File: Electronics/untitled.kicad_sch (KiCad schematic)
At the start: 23 parts

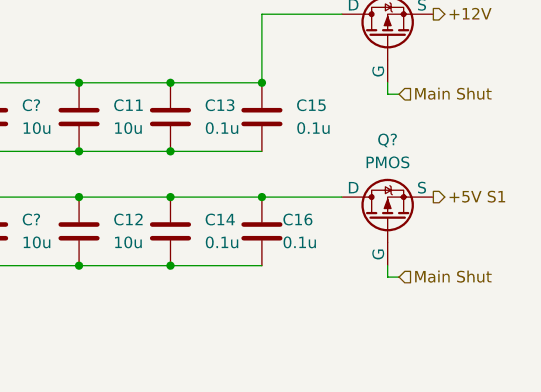
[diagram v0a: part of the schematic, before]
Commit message: Starting the Sheet connections
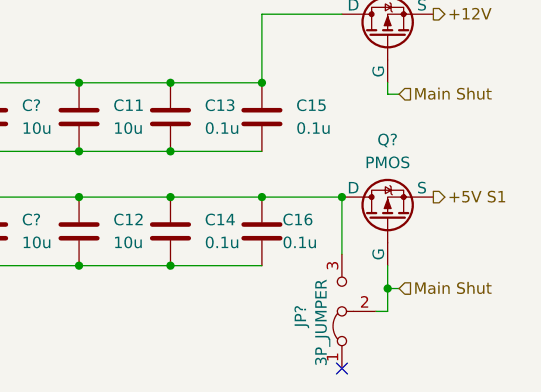
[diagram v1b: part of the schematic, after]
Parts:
- added JP?: 3P_JUMPER, symbol Jumper:Jumper_3_Bridged12
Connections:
- net Main Shut: now also JP?.2 (C)
- net at C12.1, C14.1, C16.1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: now also JP?.3 (B)
- no-connect marks 0 -> 1
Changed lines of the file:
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@@
 	(paper "A5")
 	(junction
+		(at 176.53 63.5)
+		(diameter 0)
+		(color 0 0 0 0)
+	)
+	(junction
 		(at 152.4 48.26)
 		(diameter 0)
@@
 	)
 	(junction
+		(at 171.45 53.34)
+		(diameter 0)
+		(color 0 0 0 0)
+	)
+	(junction
 		(at 121.92 40.64)
 		(diameter 0)
@@
 		(color 0 0 0 0)
 	)
+	(no_connect
+		(at 171.45 72.39)
+	)
 	(wire
 		(pts
@@
 	(wire
 		(pts
+			(xy 176.53 63.5) (xy 176.53 66.04)
+		)
+		(stroke
+			(width 0)
+			(type default)
+		)
+	)
+	(wire
+		(pts
 			(xy 121.92 40.64) (xy 111.76 40.64)
 		)
@@
 	(wire
 		(pts
+			(xy 171.45 59.69) (xy 171.45 53.34)
+		)
+		(stroke
+			(width 0)
+			(type default)
+		)
+	)
+	(wire
+		(pts
 			(xy 62.23 55.88) (xy 62.23 45.72)
 		)
@@
 	(wire
 		(pts
-			(xy 176.53 62.23) (xy 177.8 62.23)
+			(xy 176.53 63.5) (xy 177.8 63.5)
 		)
 		(stroke
@@
 	(wire
 		(pts
-			(xy 176.53 60.96) (xy 176.53 62.23)
+			(xy 176.53 60.96) (xy 176.53 63.5)
 		)
 		(stroke
@@
 		(pts
 			(xy 78.74 60.96) (xy 90.17 60.96)
+		)
+		(stroke
+			(width 0)
+			(type default)
+		)
+	)
+	(wire
+		(pts
+			(xy 176.53 66.04) (xy 175.26 66.04)
 		)
 		(stroke
@@
 	(hierarchical_label "Main Shut"
 		(shape input)
-		(at 177.8 62.23 0)
+		(at 177.8 63.5 0)
 		(effects
 			(font
@@
 		(on_board yes)
 		(dnp no)
-		(fields_autoplaced yes)
 		(property "Reference" "J?"
 			(at 52.07 33.02 0)
@@
 					(unit 1)
 				)
+			)
+		)
+	)
+	(symbol
+		(lib_id "Jumper:Jumper_3_Bridged12")
+		(at 171.45 66.04 90)
+		(unit 1)
+		(exclude_from_sim no)
+		(in_bom no)
+		(on_board yes)
+		(dnp no)
+		(property "Reference" "JP?"
+			(at 166.878 67.818 0)
+			(effects
+				(font
+					(size 1.27 1.27)
+				)
+				(justify left)
+			)
+		)
+		(property "Value" "3P_JUMPER"
+			(at 169.164 72.136 0)
+			(effects
+				(font
+					(size 1.27 1.27)
+				)
+				(justify left)
+			)
+		)
+		(property "Footprint" ""
+			(at 171.45 66.04 0)
+			(effects
+				(font
+					(size 1.27 1.27)
+				)
+				(hide yes)
+			)
+		)
+		(property "Datasheet" "~"
+			(at 171.45 66.04 0)
+			(effects
+				(font
+					(size 1.27 1.27)
+				)
+				(hide yes)
+			)
+		)
+		(property "Description" "Jumper, 3-pole, pins 1+2 closed/bridged"
+			(at 171.45 66.04 0)
+			(effects
+				(font
+					(size 1.27 1.27)
+				)
+				(hide yes)
+			)
+		)
+		(pin "3"
+		)
+		(pin "1"
+		)
+		(pin "2"
+		)
+		(instances
+			(project "CM5 Nas"
+				(path "/0650c7a8-acba-429c-9f8e-eec0baf0bc1c/fede4c36-00cc-4d3d-b71c-5243ba232202/ff10faca-55ce-4526-b63b-58be6b3f0345"
+					(reference "JP?")
+					(unit 1)
+				)

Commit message: Footprints Selected
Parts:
- removed JP?: 3P_JUMPER, symbol Jumper:Jumper_3_Bridged12
- added D5, D6: LED Green, LED_SMD:LED_0603_1608Metric, symbol Device:LED
- added R11, R12: 1K, Resistor_SMD:R_0603_1608Metric, symbol Device:R_Small
- added TP5: TestPoint, TestPoint:TestPoint_Pad_1.0x1.0mm, symbol Connector:TestPoint
- C10, C12, C13, C8: renamed from C?; footprint (none) -> Capacitor_SMD:C_0603_1608Metric
- C11: renamed from C8; footprint (none) -> Capacitor_SMD:C_0603_1608Metric
- C14: renamed from C11; footprint (none) -> Capacitor_SMD:C_0603_1608Metric
- C15: renamed from C12; footprint (none) -> Capacitor_SMD:C_0603_1608Metric
- C16: renamed from C13; footprint (none) -> Capacitor_SMD:C_0603_1608Metric
- C17: renamed from C14; footprint (none) -> Capacitor_SMD:C_0603_1608Metric
- C18: renamed from C15; footprint (none) -> Capacitor_SMD:C_0603_1608Metric
- C19: renamed from C16; footprint (none) -> Capacitor_SMD:C_0603_1608Metric
- C4: renamed from C1; value 1000n -> 1u; footprint (none) -> Capacitor_SMD:C_0603_1608Metric
- C5: renamed from C2; value 1000n -> 1u; footprint (none) -> Capacitor_SMD:C_0603_1608Metric
- C6: renamed from C3; footprint (none) -> Capacitor_SMD:C_0603_1608Metric
- C7: renamed from C4; footprint (none) -> Capacitor_SMD:C_0603_1608Metric
- C9: renamed from C6; footprint (none) -> Capacitor_SMD:C_0603_1608Metric
- D3: renamed from D1; footprint (none) -> SMBJ12A:SMBJ12A
- D4: renamed from D2; footprint (none) -> SMBJ5.0A:SMBJ5.0A
- F1, F2: footprint (none) -> RGEF1200:RGEF1200
- J15: renamed from J?; footprint 4DBP10803 -> 4DB-P108-03:4DBP10803
- Q2, Q3: renamed from Q?; footprint (none) -> IRF7425TRPBF:SOIC127P600X175-8N
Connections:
- net +12V: now also C10.1, C12.1, C14.1, C16.1, C18.1, C4.1, C6.1, C8.1, D3.2 (A2), F1.2, R11.2, TP5.1; no longer Q2.3 (S)
- net +5V S1: now also C11.1, C13.1, C15.1, C17.1, C19.1, C5.1, C7.1, C9.1, D4.2 (A2), F2.2; no longer Q3.3 (S)
- net at C11.2, C13.2, C15.2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: now also R12.2
- net at J15.2: now also Q3.1 (D); no longer F2.1
- net at J15.3: now also Q2.1 (D); no longer F1.1
- new net: D5.2 (A), R11.1
- new net: D6.2 (A), R12.1
- new net: F2.1, Q3.3 (S)
- new net: F1.1, Q2.3 (S)
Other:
- moved on the sheet: J15, Q2, Q3

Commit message: Footprints selected, Hiracicle connections created, Pcb next
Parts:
- removed C6, C7: 1000u, Capacitor_SMD:C_0603_1608Metric, symbol Device:C
- removed Q2, Q3: PMOS, IRF7425TRPBF:SOIC127P600X175-8N, symbol Simulation_SPICE:PMOS
- added C13, C5: 1000u, EEE0JA152UAP:EEE0JA152UAP, symbol Device:C_Polarized
- added TP4, TP5: TestPoint, TestPoint:TestPoint_Pad_1.0x1.0mm, symbol Connector:TestPoint
- C10: renamed from C16; value 0.1u -> 100n; footprint Capacitor_SMD:C_0603_1608Metric -> Capacitor_SMD:C_0402_1005Metric
- C11: renamed from C18; value 0.1u -> 100n; footprint Capacitor_SMD:C_0603_1608Metric -> Capacitor_SMD:C_0402_1005Metric
- C12: renamed from C5; footprint Capacitor_SMD:C_0603_1608Metric -> Capacitor_SMD:C_1210_3225Metric
- C14: renamed from C9; footprint Capacitor_SMD:C_0603_1608Metric -> Capacitor_SMD:C_1210_3225Metric
- C15: renamed from C11; footprint Capacitor_SMD:C_0603_1608Metric -> Capacitor_SMD:C_1210_3225Metric
- C16: renamed from C13; footprint Capacitor_SMD:C_0603_1608Metric -> Capacitor_SMD:C_1210_3225Metric
- C17: renamed from C15; footprint Capacitor_SMD:C_0603_1608Metric -> Capacitor_SMD:C_1210_3225Metric
- C18: renamed from C17; value 0.1u -> 100n; footprint Capacitor_SMD:C_0603_1608Metric -> Capacitor_SMD:C_0402_1005Metric
- C19: value 0.1u -> 100n; footprint Capacitor_SMD:C_0603_1608Metric -> Capacitor_SMD:C_0402_1005Metric
- C4: footprint Capacitor_SMD:C_0603_1608Metric -> Capacitor_SMD:C_1210_3225Metric
- C6: renamed from C8; footprint Capacitor_SMD:C_0603_1608Metric -> Capacitor_SMD:C_1210_3225Metric
- C7: renamed from C10; footprint Capacitor_SMD:C_0603_1608Metric -> Capacitor_SMD:C_1210_3225Metric
- C8: renamed from C12; footprint Capacitor_SMD:C_0603_1608Metric -> Capacitor_SMD:C_1210_3225Metric
- C9: renamed from C14; footprint Capacitor_SMD:C_0603_1608Metric -> Capacitor_SMD:C_1210_3225Metric
- R11: value 1K -> 2K2
- R12: value 1K -> 620
- TP3: renamed from TP5; now not fitted; now left out of the parts list
- renumbered D5 to D3, D3 to D4, D4 to D5
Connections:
- net +12V: now also C5.1; no longer TP3.1
- net +5V S1: now also C13.1
- net gnd: now reaches C10.2, C11.2, C4.2, C6.2, C7.2, C8.2, C9.2, D4.1 (A1)
- net gnd: now also C12.2, C14.2, C15.2, C16.2, C17.2, C18.2, C19.2, D3.1 (K), D5.1 (A1), D6.1 (K), J15.1, R12.2, C13.2, C5.2, TP5.1
- net at J15.2: now also F2.1, TP4.1
- net at J15.3: now also F1.1, TP3.1
- no-connect marks 1 -> 0
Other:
- moved on the sheet: J15

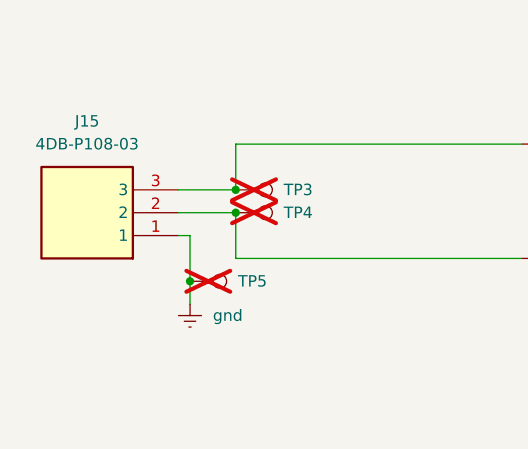
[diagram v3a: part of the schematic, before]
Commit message: Sata Port Changed
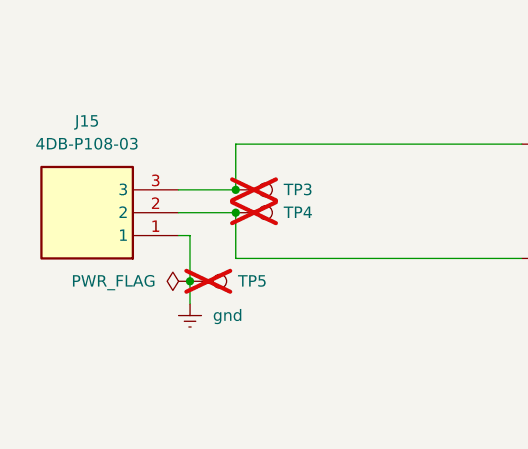
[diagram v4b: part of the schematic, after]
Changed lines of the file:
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@@
+	)
+	(symbol
+		(lib_id "power:PWR_FLAG")
+		(at 31.75 55.88 90)
+		(unit 1)
+		(exclude_from_sim no)
+		(in_bom yes)
+		(on_board yes)
+		(dnp no)
+		(fields_autoplaced yes)
+		(property "Reference" "#FLG09"
+			(at 29.845 55.88 0)
+			(effects
+				(font
+					(size 1.27 1.27)
+				)
+				(hide yes)
+			)
+		)
+		(property "Value" "PWR_FLAG"
+			(at 27.94 55.8799 90)
+			(effects
+				(font
+					(size 1.27 1.27)
+				)
+				(justify left)
+			)
+		)
+		(property "Footprint" ""
+			(at 31.75 55.88 0)
+			(effects
+				(font
+					(size 1.27 1.27)
+				)
+				(hide yes)
+			)
+		)
+		(property "Datasheet" "~"
+			(at 31.75 55.88 0)
+			(effects
+				(font
+					(size 1.27 1.27)
+				)
+				(hide yes)
+			)
+		)
+		(property "Description" "Special symbol for telling ERC where power comes from"
+			(at 31.75 55.88 0)
+			(effects
+				(font
+					(size 1.27 1.27)
+				)
+				(hide yes)
+			)
+		)
+		(pin "1"
+		)
+		(instances
+			(project "CM5 Nas"
+				(path "/0650c7a8-acba-429c-9f8e-eec0baf0bc1c/fede4c36-00cc-4d3d-b71c-5243ba232202/ff10faca-55ce-4526-b63b-58be6b3f0345"
+					(reference "#FLG09")
+					(unit 1)
+				)
+			)
+		)
 	)
 	(symbol

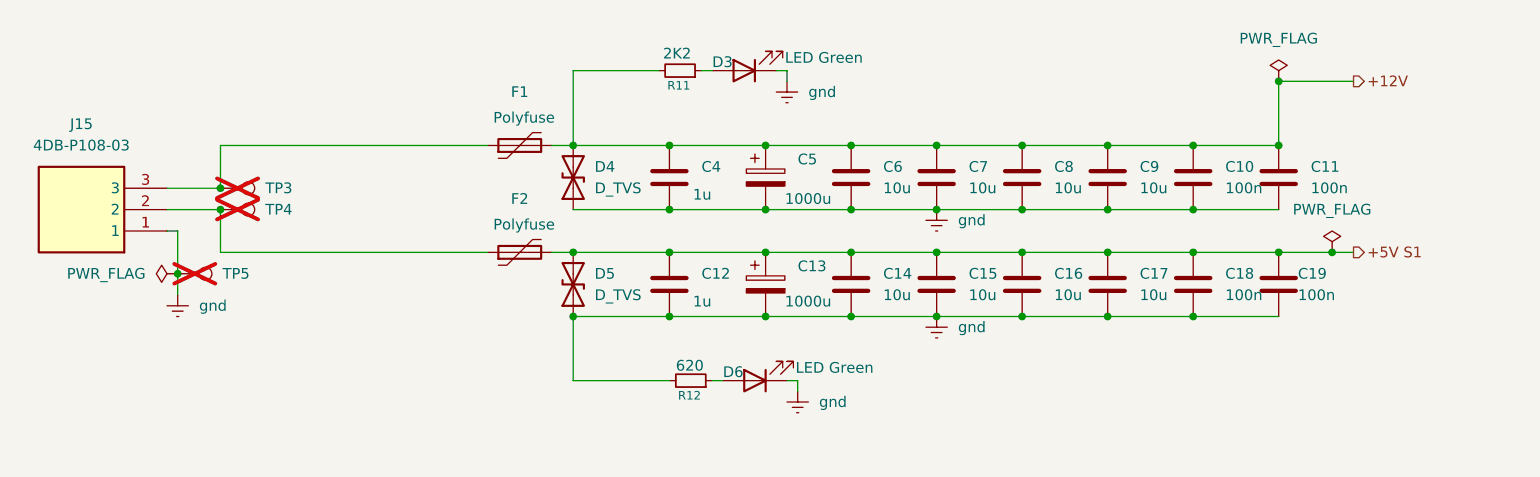
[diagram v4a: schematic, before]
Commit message: Changed sata port
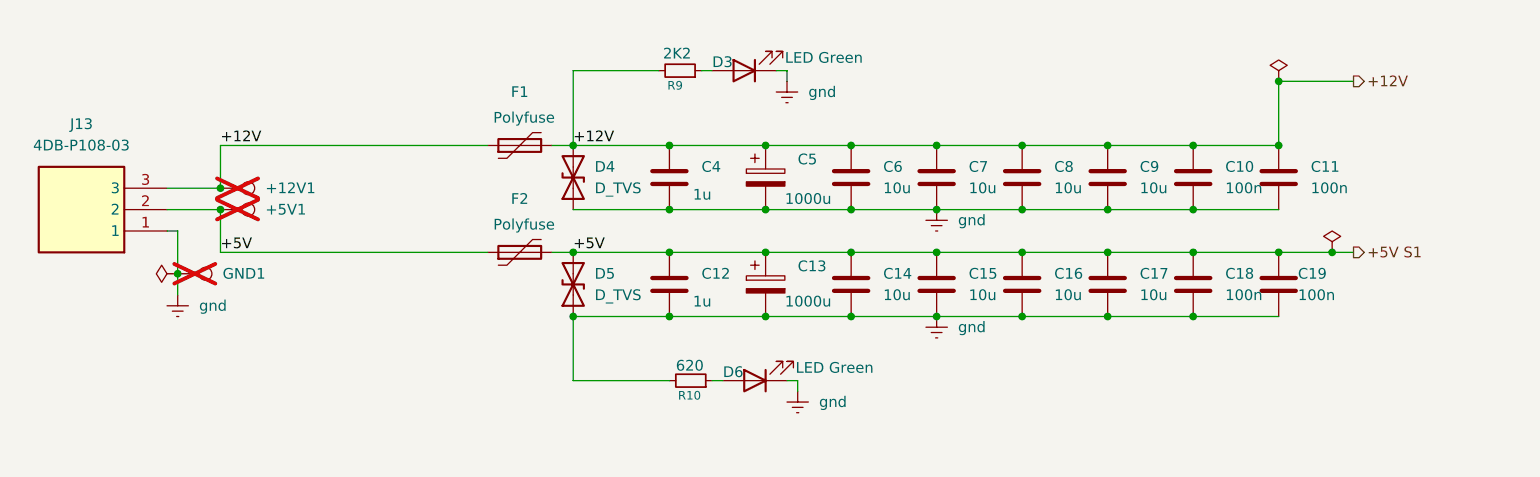
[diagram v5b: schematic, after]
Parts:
- renumbered TP3 to +12V1, TP4 to +5V1, TP5 to GND1, J15 to J13, R12 to R10, R11 to R9
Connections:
- net +12V: now also +12V1.1, F1.1, J13.3
- net +5V S1: now also +5V1.1, F2.1, J13.2
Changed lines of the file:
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@@
 	)
 	(junction
-		(at 78.74 53.34)
-		(diameter 0)
-		(color 0 0 0 0)
-	)
-	(junction
 		(at 90.17 48.26)
 		(diameter 0)
@@
 	)
 	(junction
+		(at 78.74 53.34)
+		(diameter 0)
+		(color 0 0 0 0)
+	)
+	(junction
 		(at 132.08 60.96)
 		(diameter 0)
@@
 	(wire
 		(pts
-			(xy 78.74 53.34) (xy 90.17 53.34)
-		)
-		(stroke
-			(width 0)
-			(type default)
-		)
-	)
-	(wire
-		(pts
 			(xy 105.41 68.58) (xy 104.14 68.58)
 		)
@@
 	(wire
 		(pts
+			(xy 78.74 53.34) (xy 90.17 53.34)
+		)
+		(stroke
+			(width 0)
+			(type default)
+		)
+	)
+	(wire
+		(pts
 			(xy 152.4 48.26) (xy 162.56 48.26)
 		)
@@
 		)
 	)
+	(label "+5V"
+		(at 36.83 53.34 0)
+		(effects
+			(font
+				(size 1.27 1.27)
+			)
+			(justify left bottom)
+		)
+	)
+	(label "+12V"
+		(at 36.83 40.64 0)
+		(effects
+			(font
+				(size 1.27 1.27)
+			)
+			(justify left bottom)
+		)
+	)
+	(label "+5V"
+		(at 78.74 53.34 0)
+		(effects
+			(font
+				(size 1.27 1.27)
+			)
+			(justify left bottom)
+		)
+	)
+	(label "+12V"
+		(at 78.74 40.64 0)
+		(effects
+			(font
+				(size 1.27 1.27)
+			)
+			(justify left bottom)
+		)
+	)
 	(hierarchical_label "+5V S1"
 		(shape output)
@@
 		)
 	)
+	(netclass_flag ""
+		(length 2.54)
+		(shape round)
+		(at 44.45 40.64 0)
+		(fields_autoplaced yes)
+		(effects
+			(font
+				(size 1.27 1.27)
+			)
+			(justify left bottom)
+		)
+		(property "Netclass" "PWR RAIL"
+			(at 45.1485 38.1 0)
+			(effects
+				(font
+					(size 1.27 1.27)
+				)
+				(justify left)
+			)
+		)
+		(property "Component Class" ""
+			(at -177.8 55.88 0)
+			(effects
+				(font
+					(size 1.27 1.27)
+					(italic yes)
+				)
+			)
+		)
+	)
+	(netclass_flag ""
+		(length 2.54)
+		(shape round)
+		(at 44.45 53.34 0)
+		(fields_autoplaced yes)
+		(effects
+			(font
+				(size 1.27 1.27)
+			)
+			(justify left bottom)
+		)
+		(property "Netclass" "PWR RAIL"
+			(at 45.1485 50.8 0)
+			(effects
+				(font
+					(size 1.27 1.27)
+				)
+				(justify left)
+			)
+		)
+		(property "Component Class" ""
+			(at -25.4 27.94 0)
+			(effects
+				(font
+					(size 1.27 1.27)
+					(italic yes)
+				)
+			)
+		)
+	)
 	(symbol
 		(lib_id "Device:R_Small")
@@
 		(on_board yes)
 		(dnp no)
-		(property "Reference" "R11"
+		(property "Reference" "R9"
 			(at 89.916 33.528 90)
 			(effects
@@
 			(project "CM5 Nas"
 				(path "/0650c7a8-acba-429c-9f8e-eec0baf0bc1c/fede4c36-00cc-4d3d-b71c-5243ba232202/ff10faca-55ce-4526-b63b-58be6b3f0345"
-					(reference "R11")
+					(reference "R9")
 					(unit 1)
 				)
@@
 		(dnp no)
 		(fields_autoplaced yes)
-		(property "Reference" "#PWR032"
+		(property "Reference" "#PWR026"
 			(at 31.75 64.77 0)
 			(effects
@@
 			(project "CM5 Nas"
 				(path "/0650c7a8-acba-429c-9f8e-eec0baf0bc1c/fede4c36-00cc-4d3d-b71c-5243ba232202/ff10faca-55ce-4526-b63b-58be6b3f0345"
-					(reference "#PWR032")
+					(reference "#PWR026")
 					(unit 1)
 				)
@@
 					(size 1.27 1.27)
 				)
+				(hide yes)
 			)
 		)
@@
 		(on_board yes)
 		(dnp yes)
-		(property "Reference" "TP3"
+		(property "Reference" "+12V1"
 			(at 42.164 45.72 90)
 			(effects
@@
 			(project "CM5 Nas"
 				(path "/0650c7a8-acba-429c-9f8e-eec0baf0bc1c/fede4c36-00cc-4d3d-b71c-5243ba232202/ff10faca-55ce-4526-b63b-58be6b3f0345"
-					(reference "TP3")
+					(reference "+12V1")
 					(unit 1)
 				)
@@
 		(dnp no)
 		(fields_autoplaced yes)
-		(property "Reference" "#PWR030"
+		(property "Reference" "#PWR024"
 			(at 104.14 39.37 0)
 			(effects
@@
 			(project "CM5 Nas"
 				(path "/0650c7a8-acba-429c-9f8e-eec0baf0bc1c/fede4c36-00cc-4d3d-b71c-5243ba232202/ff10faca-55ce-4526-b63b-58be6b3f0345"
-					(reference "#PWR030")
+					(reference "#PWR024")
 					(unit 1)
 				)
@@
 		(on_board yes)
 		(dnp yes)
-		(property "Reference" "TP4"
+		(property "Reference" "+5V1"
 			(at 42.164 48.26 90)
 			(effects
@@
 			(project "CM5 Nas"
 				(path "/0650c7a8-acba-429c-9f8e-eec0baf0bc1c/fede4c36-00cc-4d3d-b71c-5243ba232202/ff10faca-55ce-4526-b63b-58be6b3f0345"
-					(reference "TP4")
+					(reference "+5V1")
 					(unit 1)
 				)
@@
 		(dnp no)
 		(fields_autoplaced yes)
-		(property "Reference" "#PWR033"
+		(property "Reference" "#PWR027"
 			(at 121.92 67.31 0)
 			(effects
@@
 			(project "CM5 Nas"
 				(path "/0650c7a8-acba-429c-9f8e-eec0baf0bc1c/fede4c36-00cc-4d3d-b71c-5243ba232202/ff10faca-55ce-4526-b63b-58be6b3f0345"
-					(reference "#PWR033")
+					(reference "#PWR027")
 					(unit 1)
 				)
@@
 		(on_board yes)
 		(dnp yes)
-		(property "Reference" "TP5"
+		(property "Reference" "GND1"
 			(at 37.084 55.88 90)
 			(effects
@@
 			(project "CM5 Nas"
 				(path "/0650c7a8-acba-429c-9f8e-eec0baf0bc1c/fede4c36-00cc-4d3d-b71c-5243ba232202/ff10faca-55ce-4526-b63b-58be6b3f0345"
-					(reference "TP5")
+					(reference "GND1")
 					(unit 1)
 				)
@@
 		(dnp no)
 		(fields_autoplaced yes)
-		(property "Reference" "#PWR034"
+		(property "Reference" "#PWR028"
 			(at 105.41 76.2 0)
 			(effects
@@
 			(project "CM5 Nas"
 				(path "/0650c7a8-acba-429c-9f8e-eec0baf0bc1c/fede4c36-00cc-4d3d-b71c-5243ba232202/ff10faca-55ce-4526-b63b-58be6b3f0345"
-					(reference "#PWR034")
+					(reference "#PWR028")
 					(unit 1)
 				)
@@
 		(on_board yes)
 		(dnp no)
-		(property "Reference" "J15"
+		(property "Reference" "J13"
 			(at 20.32 38.1 0)
 			(effects
@@
 			(project ""
 				(path "/0650c7a8-acba-429c-9f8e-eec0baf0bc1c/fede4c36-00cc-4d3d-b71c-5243ba232202/ff10faca-55ce-4526-b63b-58be6b3f0345"
-					(reference "J15")
+					(reference "J13")
 					(unit 1)
 				)
@@
 		(dnp no)
 		(fields_autoplaced yes)
-		(property "Reference" "#PWR031"
+		(property "Reference" "#PWR025"
 			(at 121.92 54.61 0)
 			(effects
@@
 			(project "CM5 Nas"
 				(path "/0650c7a8-acba-429c-9f8e-eec0baf0bc1c/fede4c36-00cc-4d3d-b71c-5243ba232202/ff10faca-55ce-4526-b63b-58be6b3f0345"
-					(reference "#PWR031")
+					(reference "#PWR025")
 					(unit 1)
 				)
@@
 					(size 1.27 1.27)
 				)
+				(hide yes)
 			)
 		)
@@
 		(on_board yes)
 		(dnp no)
-		(property "Reference" "R12"
+		(property "Reference" "R10"
 			(at 91.186 70.358 90)
 			(effects
@@
 			(project "CM5 Nas"
 				(path "/0650c7a8-acba-429c-9f8e-eec0baf0bc1c/fede4c36-00cc-4d3d-b71c-5243ba232202/ff10faca-55ce-4526-b63b-58be6b3f0345"
-					(reference "R12")
+					(reference "R10")
 					(unit 1)
 				)
@@
 		(dnp no)
 		(fields_autoplaced yes)
-		(property "Reference" "#FLG09"
+		(property "Reference" "#FLG03"
 			(at 29.845 55.88 0)
 			(effects
@@
 				)
 				(justify left)
+				(hide yes)
 			)
 		)
@@
 			(project "CM5 Nas"
 				(path "/0650c7a8-acba-429c-9f8e-eec0baf0bc1c/fede4c36-00cc-4d3d-b71c-5243ba232202/ff10faca-55ce-4526-b63b-58be6b3f0345"
-					(reference "#FLG09")
+					(reference "#FLG03")
 					(unit 1)
 				)

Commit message: More pcbing
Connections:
- net +5V S1: no longer +5V1.1, F2.1, J13.2
- new net +5V: +5V1.1, F2.1, J13.2
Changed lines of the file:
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@@
 		)
 	)
-	(label "+5V"
+	(label "+5V S1"
 		(at 78.74 53.34 0)
 		(effects
